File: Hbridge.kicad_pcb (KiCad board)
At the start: 2 copper layers, 90 x 60 mm, 40 parts, among them J1 nodeLync IN, J2 nodeLync OUT, J3 Conn_02x05_Odd_Even, J4 Motor, J5 Power Pole, J6 Conn_02x02_Odd_Even, U1 MCP23008-E/P, U2 VNH7100BASTR, U3 MCP3427-E/UN

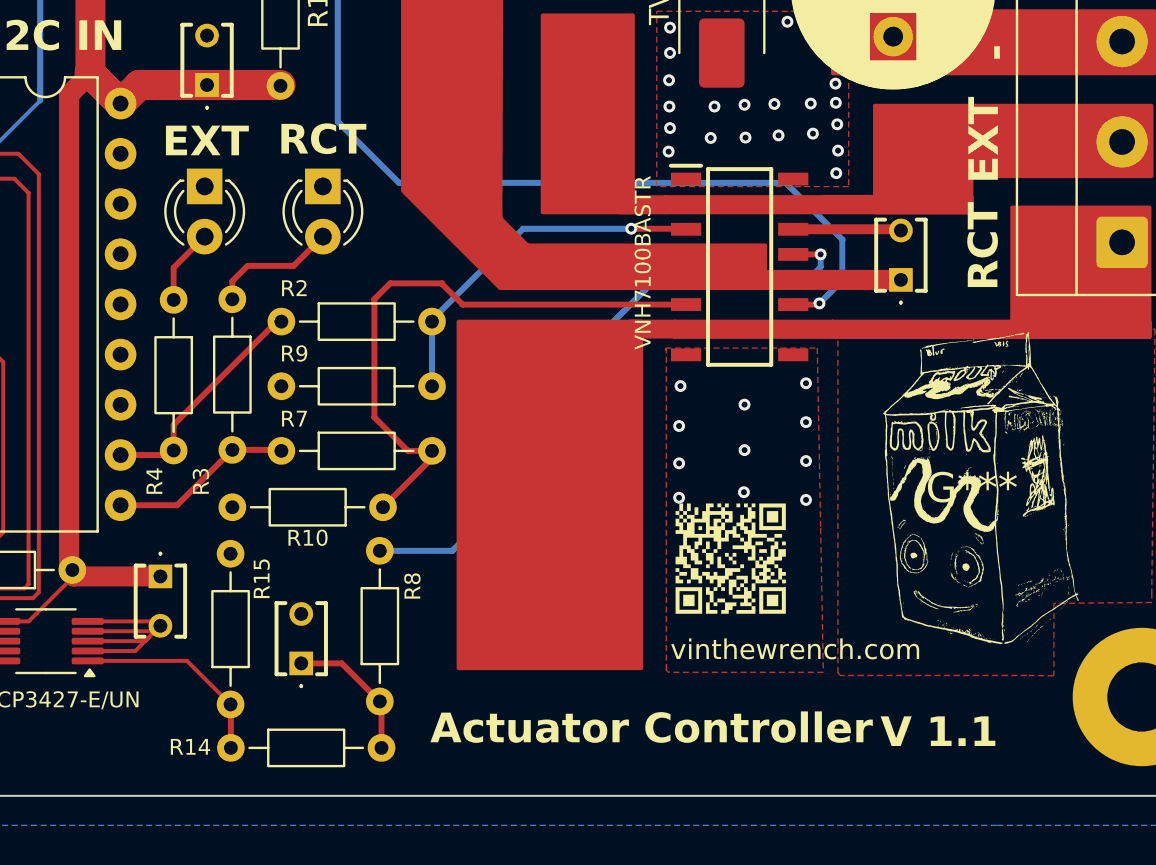
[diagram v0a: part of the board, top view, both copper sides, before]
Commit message: corrected issues with sense resistor for CS and SEL
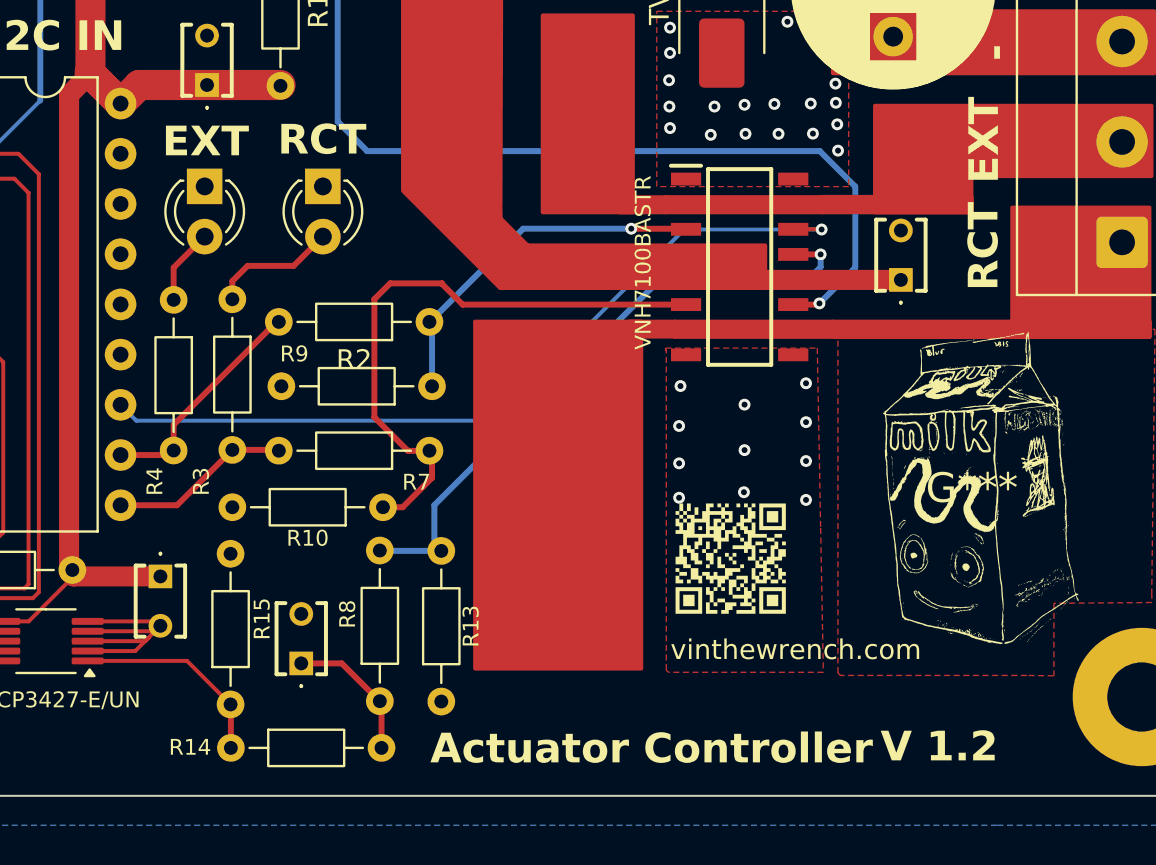
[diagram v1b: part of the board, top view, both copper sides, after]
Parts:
- added R13: 1K, Resistor_THT:R_Axial_DIN0204_L3.6mm_D1.6mm_P7.62mm_Horizontal, F.Cu at (69.6, 75.2)
- R14: value 10K -> 3K
- R15: value 10K -> 1K
- R3: value 4.7K -> 300
- moved R2 7.49 mm to (69.0, 56.0), turned to 180 degrees
- moved R7 7.49 mm to (69.0, 62.5), turned to 180 degrees
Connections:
- R2 pad 1: /EXTEND -> Net-(U2-INA)
- R2 pad 2: Net-(U2-INA) -> /EXTEND
- R7 pad 1: /RETRACT -> Net-(U2-INB)
- R7 pad 2: Net-(U2-INB) -> /RETRACT
- U1 pad 12: unconnected-(U1-GP2-Pad12) -> /SEL
- U2 pad 14: GND1 -> /SEL
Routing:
- net /SEL: track 0.00 -> 41.2 mm, vias 0 -> 1
- net GND1: track 32.6 -> 27.2 mm, vias 32 -> 30
- net Net-(U2-PWM): track 43.6 -> 46.1 mm
- net Net-(U2-CS): track 32.3 -> 31.6 mm
- net Net-(U2-INB): track 29.7 -> 30.2 mm
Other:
- board text added: "V 1.2"
- board text removed: "V 1.1"
